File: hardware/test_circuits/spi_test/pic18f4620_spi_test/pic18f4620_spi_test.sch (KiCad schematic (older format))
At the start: 44 parts, among them J1 Conn_01x05_Female, J2 Conn_01x05_Female, SW1 SW_Push, SW2 SW_Push, SW3 SW_SPDT, U1 PIC18F4620-IP, U2 L7805, U3 PIC18F4620-IP, Y1 10MHz, Y2 10MHz

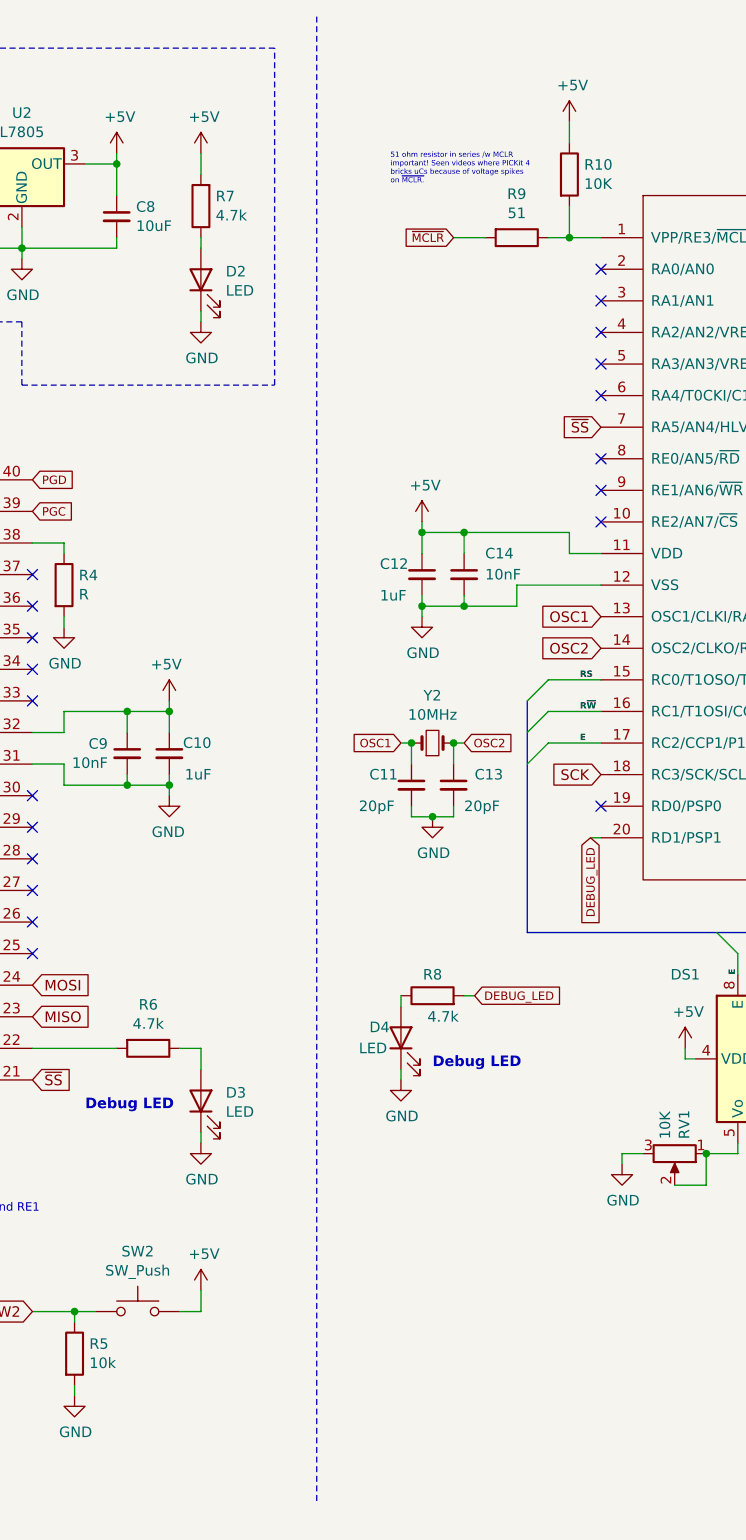
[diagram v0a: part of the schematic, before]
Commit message: Finished CAN Test schematic now. Also added schematics for the individual elements used so that it would make it easier to reuse for later schematics!
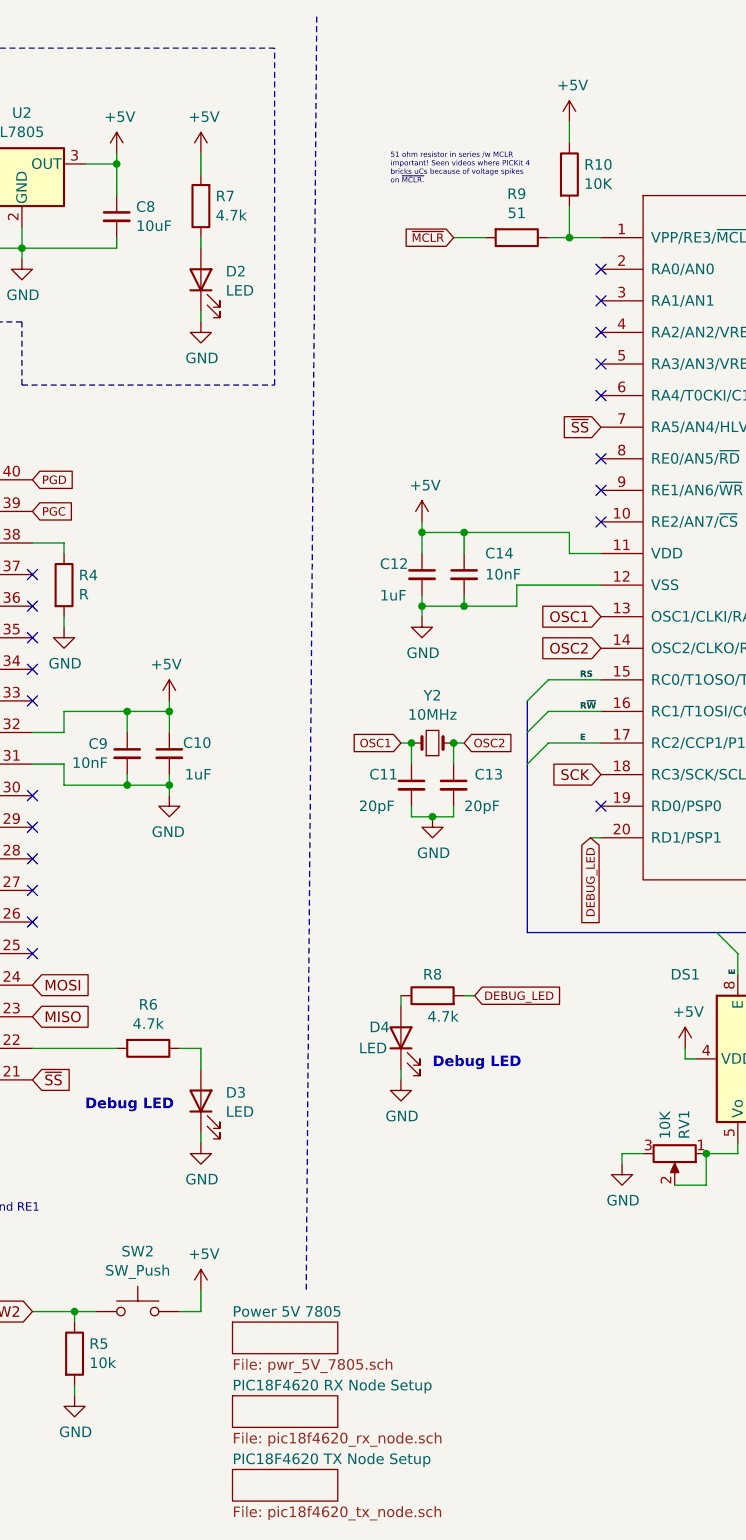
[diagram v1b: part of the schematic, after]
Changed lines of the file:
@@
 $Descr A4 11693 8268
 encoding utf-8
-Sheet 1 1
+Sheet 1 4
 Title "PIC18F4620 - MSSP SPI Test Circuit"
 Date "2021-11-04"
-Rev "Ver. 1"
+Rev "1.0"
 Comp "Personal Project"
 Comment1 ""
@@
 Use with something like\na PICkit4.
 Wire Notes Line
-	5950 550  5950 7600
+	5950 550  5900 6600
 $Comp
 L can_node_board_hw:PIC18F4620-IP U3
@@
 Text GLabel 2150 4700 0    40   Input ~ 0
 OSC2
+$Comp
+L Switch:SW_SPDT SW3
+U 1 1 61D41444
+P 3300 1400
+F 0 "SW3" H 3250 1550 50  0000 C CNN
+F 1 "SW_SPDT" H 3150 1250 50  0000 C CNN
+F 2 "" H 3300 1400 50  0001 C CNN
+F 3 "~" H 3300 1400 50  0001 C CNN
+	1    3300 1400
+	1    0    0    -1
+$EndComp
+$Comp
+L power:VPP #PWR010
+U 1 1 6185940E
+P 3000 1200
+F 0 "#PWR010" H 3000 1050 50  0001 C CNN
+F 1 "VPP" H 3015 1373 50  0000 C CNN
+F 2 "" H 3000 1200 50  0001 C CNN
+F 3 "" H 3000 1200 50  0001 C CNN
+	1    3000 1200
+	1    0    0    -1
+$EndComp
+$Sheet
+S 5550 7450 500  150
+U 619FAD4D
+F0 "PIC18F4620 TX Node Setup" 50
+F1 "pic18f4620_tx_node.sch" 50
+$EndSheet
+$Sheet
+S 5550 7100 500  150
+U 61A0C441
+F0 "PIC18F4620 RX Node Setup" 50
+F1 "pic18f4620_rx_node.sch" 50
+$EndSheet
+$Sheet
+S 5550 6750 500  150
+U 61A1D4A2
+F0 "Power 5V 7805" 50
+F1 "pwr_5V_7805.sch" 50
+$EndSheet
 Wire Bus Line
 	6950 3800 6950 4900
@@
 Wire Bus Line
 	9950 3200 9950 3850
-$Comp
-L Switch:SW_SPDT SW3
-U 1 1 61D41444
-P 3300 1400
-F 0 "SW3" H 3250 1550 50  0000 C CNN
-F 1 "SW_SPDT" H 3150 1250 50  0000 C CNN
-F 2 "" H 3300 1400 50  0001 C CNN
-F 3 "~" H 3300 1400 50  0001 C CNN
-	1    3300 1400
-	1    0    0    -1
-$EndComp
-$Comp
-L power:VPP #PWR010
-U 1 1 6185940E
-P 3000 1200
-F 0 "#PWR010" H 3000 1050 50  0001 C CNN
-F 1 "VPP" H 3015 1373 50  0000 C CNN
-F 2 "" H 3000 1200 50  0001 C CNN
-F 3 "" H 3000 1200 50  0001 C CNN
-	1    3000 1200
-	1    0    0    -1
-$EndComp
 $EndSCHEMATC

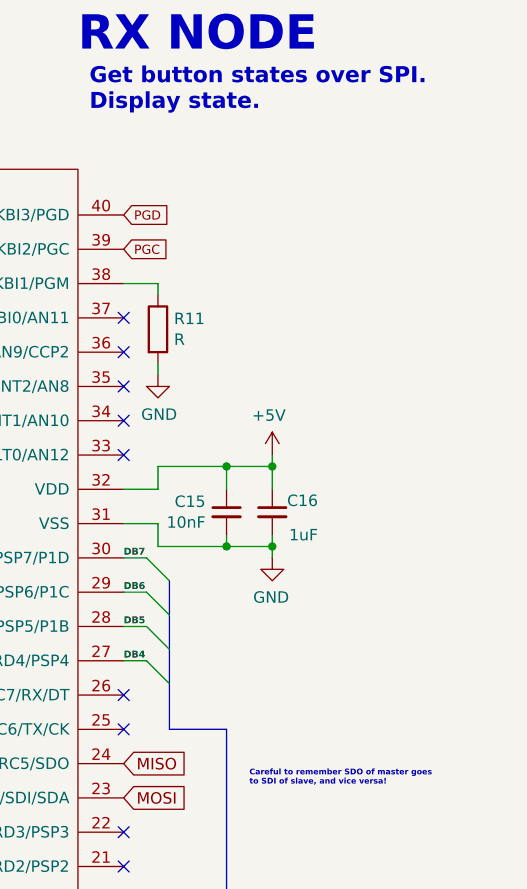
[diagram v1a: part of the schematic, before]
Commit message: Completed draft the mcp2515.h and did minor edits to schematics.
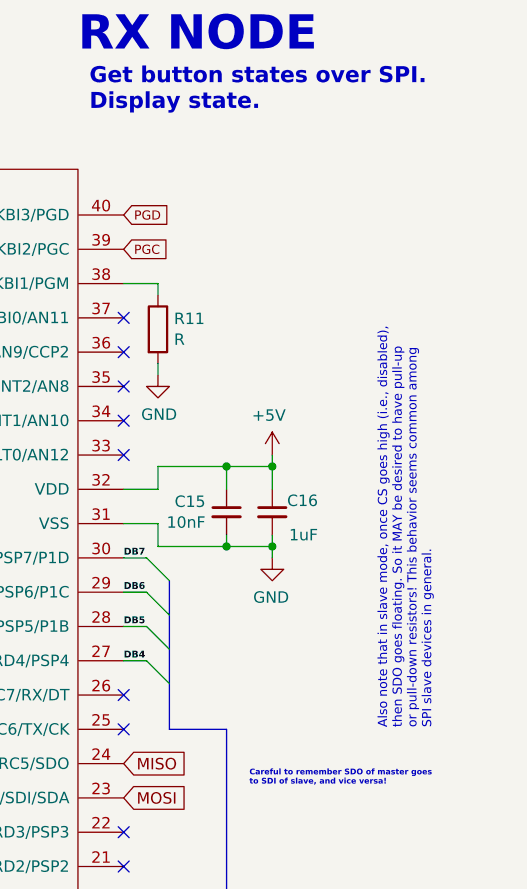
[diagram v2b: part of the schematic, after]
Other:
- note added: "Also note that in slave mode, once CS goes high (i.e., disabled),\nthen SDO goes floating. So it MAY be desired to have pull-up\nor pull-down resistors! This behavior seems common among\nSPI slave devices in general."
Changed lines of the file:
@@
 Wire Bus Line
 	9950 3200 9950 3850
+Text Notes 11100 3850 1    40   ~ 0
+Also note that in slave mode, once CS goes high (i.e., disabled),\nthen SDO goes floating. So it MAY be desired to have pull-up\nor pull-down resistors! This behavior seems common among\nSPI slave devices in general.
 $EndSCHEMATC
